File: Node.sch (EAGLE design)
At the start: 60 parts, among them J2 DF12A3.0-14DS, Q1 16MHz, U1 ATMEGA32U4QFN, U2 NRF24L01SMD, U3 LTC3553, U4 L3GD20, U6 LSM303DLHC, U7 BD2425NNRF0404, U9 RCLAMP0502A, X1 USBSMD

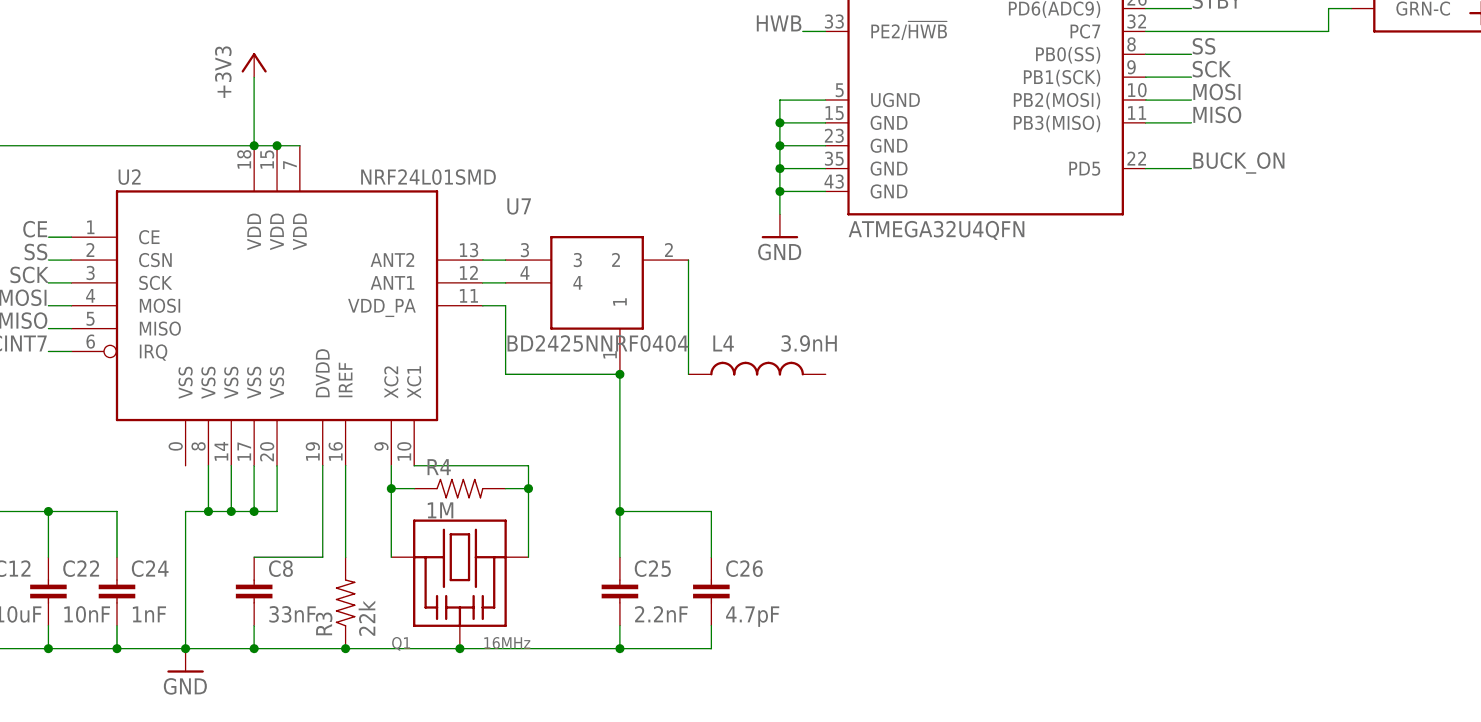
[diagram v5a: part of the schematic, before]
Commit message: add the antenna
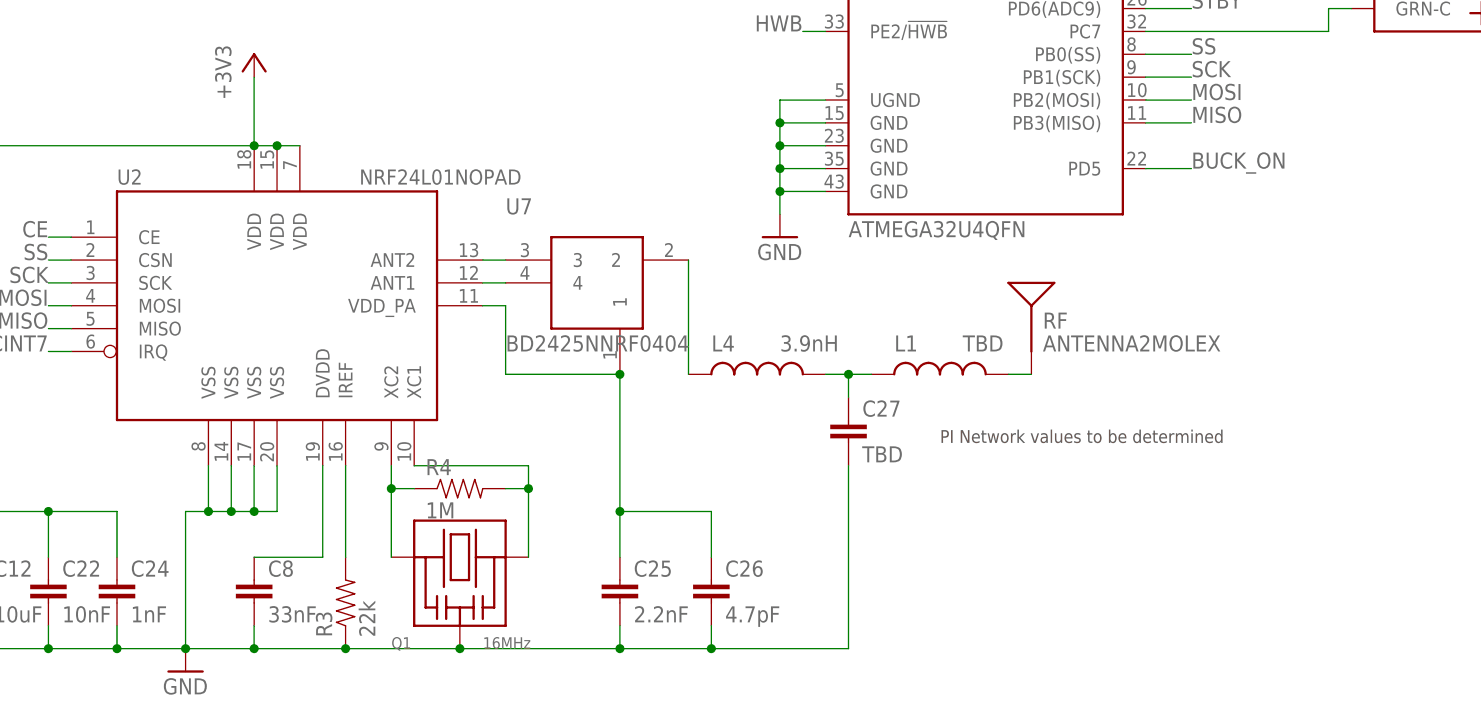
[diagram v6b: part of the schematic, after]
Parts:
- added C27: TBD, SparkFun:CAP0402-CAP
- added L1: TBD, adjacent-reality:INDUCTOR0402
- added RF: ANTENNA2MOLEX, adjacent-reality:ANTENNA2MOLEX
- U2: value NRF24L01SMD -> NRF24L01NOPAD; device SparkFun-RF:NRF24L01SMD -> adjacent-reality:NRF24L01NOPAD
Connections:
- new net N$30: L1.2, RF.SIGNAL
- new net N$31: C27.1, L1.1, L4.2
- net GND: now also C27.2
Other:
- note added: "PI Network values to be determined"
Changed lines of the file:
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@@
 <grid distance="0.1" unitdist="inch" unit="inch" style="lines" multiple="1" display="no" altdistance="0.01" altunitdist="inch" altunit="inch"/>
 <layers>
-<layer number="1" name="Top" color="4" fill="1" visible="yes" active="no"/>
-<layer number="16" name="Bottom" color="1" fill="1" visible="yes" active="no"/>
-<layer number="17" name="Pads" color="2" fill="1" visible="yes" active="no"/>
-<layer number="18" name="Vias" color="2" fill="1" visible="yes" active="no"/>
-<layer number="19" name="Unrouted" color="6" fill="1" visible="yes" active="no"/>
-<layer number="20" name="Dimension" color="15" fill="1" visible="yes" active="no"/>
-<layer number="21" name="tPlace" color="7" fill="1" visible="yes" active="no"/>
-<layer number="22" name="bPlace" color="7" fill="1" visible="yes" active="no"/>
-<layer number="23" name="tOrigins" color="15" fill="1" visible="yes" active="no"/>
-<layer number="24" name="bOrigins" color="15" fill="1" visible="yes" active="no"/>
-<layer number="25" name="tNames" color="7" fill="1" visible="yes" active="no"/>
-<layer number="26" name="bNames" color="7" fill="1" visible="yes" active="no"/>
-<layer number="27" name="tValues" color="7" fill="1" visible="yes" active="no"/>
-<layer number="28" name="bValues" color="7" fill="1" visible="yes" active="no"/>
+<layer number="1" name="Top" color="4" fill="1" visible="no" active="no"/>
+<layer number="16" name="Bottom" color="1" fill="1" visible="no" active="no"/>
+<layer number="17" name="Pads" color="2" fill="1" visible="no" active="no"/>
+<layer number="18" name="Vias" color="2" fill="1" visible="no" active="no"/>
+<layer number="19" name="Unrouted" color="6" fill="1" visible="no" active="no"/>
+<layer number="20" name="Dimension" color="15" fill="1" visible="no" active="no"/>
+<layer number="21" name="tPlace" color="7" fill="1" visible="no" active="no"/>
+<layer number="22" name="bPlace" color="7" fill="1" visible="no" active="no"/>
+<layer number="23" name="tOrigins" color="15" fill="1" visible="no" active="no"/>
+<layer number="24" name="bOrigins" color="15" fill="1" visible="no" active="no"/>
+<layer number="25" name="tNames" color="7" fill="1" visible="no" active="no"/>
+<layer number="26" name="bNames" color="7" fill="1" visible="no" active="no"/>
+<layer number="27" name="tValues" color="7" fill="1" visible="no" active="no"/>
+<layer number="28" name="bValues" color="7" fill="1" visible="no" active="no"/>
 <layer number="29" name="tStop" color="7" fill="3" visible="no" active="no"/>
 <layer number="30" name="bStop" color="7" fill="6" visible="no" active="no"/>
@@
 <layer number="35" name="tGlue" color="7" fill="4" visible="no" active="no"/>
 <layer number="36" name="bGlue" color="7" fill="5" visible="no" active="no"/>
-<layer number="37" name="tTest" color="7" fill="1" visible="yes" active="no"/>
-<layer number="38" name="bTest" color="7" fill="1" visible="yes" active="no"/>
+<layer number="37" name="tTest" color="7" fill="1" visible="no" active="no"/>
+<layer number="38" name="bTest" color="7" fill="1" visible="no" active="no"/>
 <layer number="39" name="tKeepout" color="4" fill="11" visible="no" active="no"/>
 <layer number="40" name="bKeepout" color="1" fill="11" visible="no" active="no"/>
@@
 <layer number="44" name="Drills" color="7" fill="1" visible="no" active="no"/>
 <layer number="45" name="Holes" color="7" fill="1" visible="no" active="no"/>
-<layer number="46" name="Milling" color="3" fill="1" visible="yes" active="no"/>
-<layer number="47" name="Measures" color="7" fill="1" visible="yes" active="no"/>
-<layer number="48" name="Document" color="7" fill="1" visible="yes" active="no"/>
-<layer number="49" name="Reference" color="7" fill="1" visible="yes" active="no"/>
-<layer number="50" name="dxf" color="7" fill="1" visible="yes" active="no"/>
-<layer number="51" name="tDocu" color="7" fill="1" visible="yes" active="no"/>
-<layer number="52" name="bDocu" color="7" fill="1" visible="yes" active="no"/>
-<layer number="53" name="tGND_GNDA" color="7" fill="9" visible="yes" active="no"/>
-<layer number="54" name="bGND_GNDA" color="1" fill="9" visible="yes" active="no"/>
-<layer number="56" name="wert" color="7" fill="1" visible="yes" active="no"/>
+<layer number="46" name="Milling" color="3" fill="1" visible="no" active="no"/>
+<layer number="47" name="Measures" color="7" fill="1" visible="no" active="no"/>
+<layer number="48" name="Document" color="7" fill="1" visible="no" active="no"/>
+<layer number="49" name="Reference" color="7" fill="1" visible="no" active="no"/>
+<layer number="50" name="dxf" color="7" fill="1" visible="no" active="no"/>
+<layer number="51" name="tDocu" color="7" fill="1" visible="no" active="no"/>
+<layer number="52" name="bDocu" color="7" fill="1" visible="no" active="no"/>
+<layer number="53" name="tGND_GNDA" color="7" fill="9" visible="no" active="no"/>
+<layer number="54" name="bGND_GNDA" color="1" fill="9" visible="no" active="no"/>
+<layer number="56" name="wert" color="7" fill="1" visible="no" active="no"/>
 <layer number="91" name="Nets" color="2" fill="1" visible="yes" active="yes"/>
 <layer number="92" name="Busses" color="1" fill="1" visible="yes" active="yes"/>
@@
 <part name="U3" library="adjacent-reality" deviceset="LTC3553" device=""/>
 <part name="HWB" library="SparkFun-Passives" deviceset="SOLDERJUMPER" device="NO"/>
-<part name="U2" library="SparkFun-RF" deviceset="NRF24L01" device="SMD"/>
+<part name="U2" library="adjacent-reality" deviceset="NRF24L01" device="NOPAD"/>
 <part name="+3V4" library="supply1" deviceset="+3V3" device=""/>
 <part name="GND4" library="supply1" deviceset="GND" device=""/>
@@
 <part name="L4" library="adjacent-reality" deviceset="INDUCTOR" device="0402" value="3.9nH"/>
 <part name="U7" library="adjacent-reality" deviceset="BD2425NNRF" device="0404"/>
+<part name="L1" library="adjacent-reality" deviceset="INDUCTOR" device="0402" value="TBD"/>
+<part name="C27" library="SparkFun" deviceset="CAP" device="0402-CAP" value="TBD"/>
+<part name="RF" library="adjacent-reality" deviceset="ANTENNA2" device="MOLEX"/>
 </parts>
 <sheets>
 <sheet>
 <plain>
+<text x="116.84" y="33.02" size="1.4224" layer="97" font="vector">PI Network values to be determined</text>
 </plain>
 <instances>
@@
 </instance>
 <instance part="U7" gate="G$1" x="78.74" y="50.8"/>
+<instance part="L1" gate="G$1" x="116.84" y="40.64" smashed="yes" rot="R90">
+<attribute name="NAME" x="111.76" y="43.18" size="1.778" layer="95"/>
+<attribute name="VALUE" x="119.38" y="43.18" size="1.778" layer="96"/>
+</instance>
+<instance part="C27" gate="G$1" x="106.68" y="33.02"/>
+<instance part="RF" gate="G$1" x="127" y="45.72"/>
 </instances>
 <busses>
@@
 <wire x1="91.44" y1="10.16" x2="81.28" y2="10.16" width="0.1524" layer="91"/>
 <wire x1="91.44" y1="12.7" x2="91.44" y2="10.16" width="0.1524" layer="91"/>
+<pinref part="C27" gate="G$1" pin="2"/>
+<wire x1="106.68" y1="30.48" x2="106.68" y2="10.16" width="0.1524" layer="91"/>
+<wire x1="106.68" y1="10.16" x2="91.44" y2="10.16" width="0.1524" layer="91"/>
+<junction x="91.44" y="10.16"/>
 </segment>
 <segment>
@@
 </segment>
 </net>
+<net name="N$31" class="0">
+<segment>
+<pinref part="L4" gate="G$1" pin="2"/>
+<pinref part="C27" gate="G$1" pin="1"/>
+<wire x1="104.14" y1="40.64" x2="106.68" y2="40.64" width="0.1524" layer="91"/>
+<wire x1="106.68" y1="40.64" x2="106.68" y2="38.1" width="0.1524" layer="91"/>
+<pinref part="L1" gate="G$1" pin="1"/>
+<wire x1="106.68" y1="40.64" x2="109.22" y2="40.64" width="0.1524" layer="91"/>
+<junction x="106.68" y="40.64"/>
+</segment>
+</net>
+<net name="N$30" class="0">
+<segment>
+<pinref part="L1" gate="G$1" pin="2"/>
+<pinref part="RF" gate="G$1" pin="SIGNAL"/>
+<wire x1="124.46" y1="40.64" x2="127" y2="40.64" width="0.1524" layer="91"/>
+</segment>
+</net>

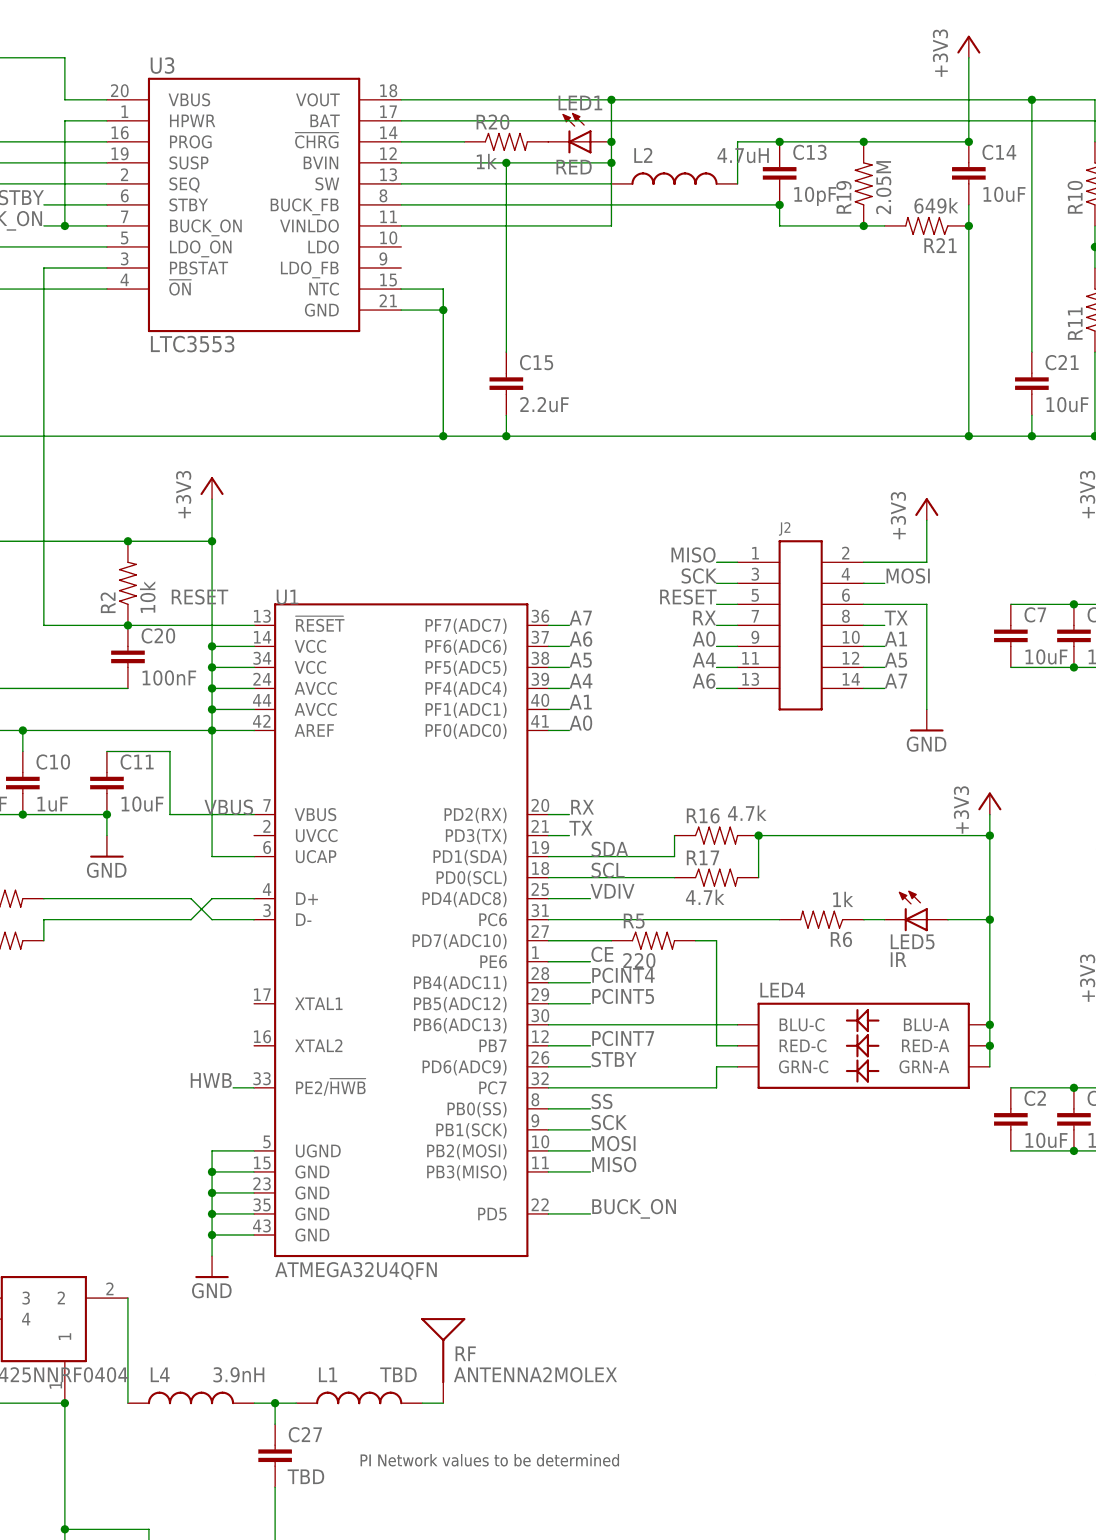
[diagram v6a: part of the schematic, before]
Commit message: cleanup some names
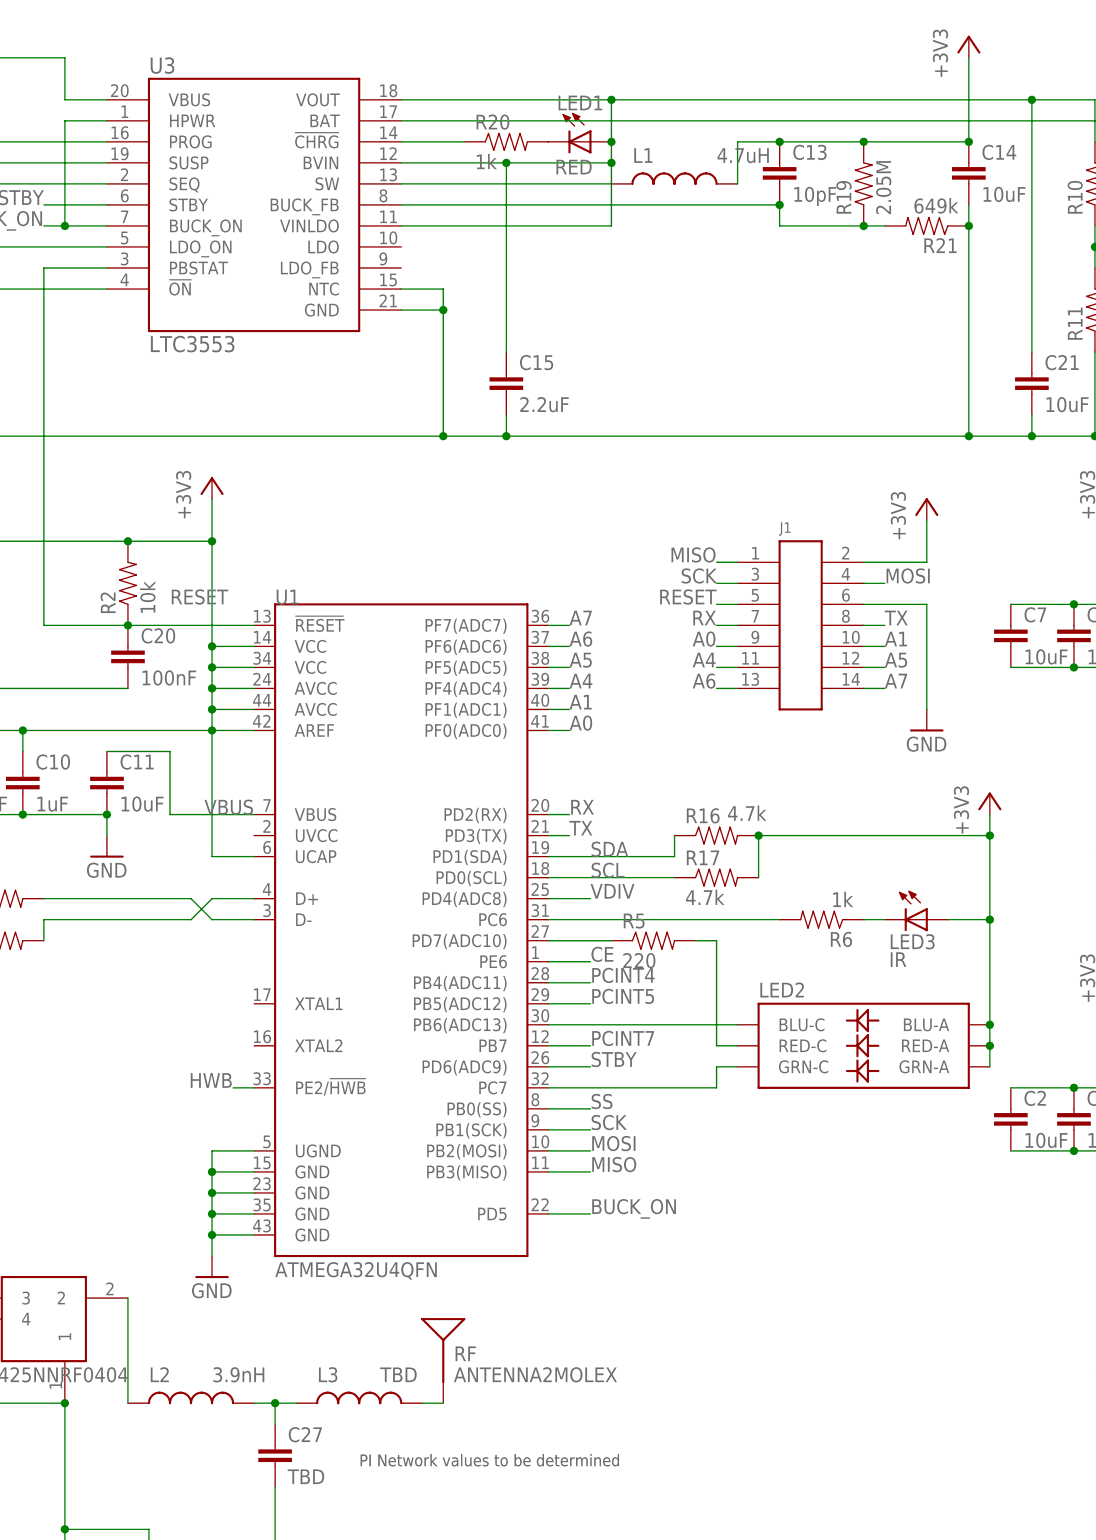
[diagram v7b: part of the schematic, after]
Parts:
- removed L4: 3.9nH, adjacent-reality:INDUCTOR0402
- added L3: TBD, adjacent-reality:INDUCTOR0402
- L1: value TBD -> 4.7uH; device adjacent-reality:INDUCTOR0402 -> adjacent-reality:INDUCTORVLS30
- L2: value 4.7uH -> 3.9nH; device adjacent-reality:INDUCTORVLS30 -> adjacent-reality:INDUCTOR0402
- renumbered J2 to J1, LED4 to LED2, LED5 to LED3
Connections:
- net +3V3: now also L1.2; no longer L2.2
- net N$27: now also L1.1; no longer L2.1
- net N$28: now also L2.1; no longer L4.1
- net N$30: now also L3.2; no longer L1.2
- net N$31: now also L2.2, L3.1; no longer L1.1, L4.2
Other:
- moved on the sheet: L1, L2
